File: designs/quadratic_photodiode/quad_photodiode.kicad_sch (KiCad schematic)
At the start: 56 parts, among them J1 Conn_Coaxial, J2 Conn_Coaxial, J3 Conn_Coaxial, J4 Conn_01x03_Female, U1 OPA356xxD, U2 OPA356xxD, U3 OPA356xxD, U4 OPA356xxD, U5 OPA356xxD, U6 OPA356xxD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

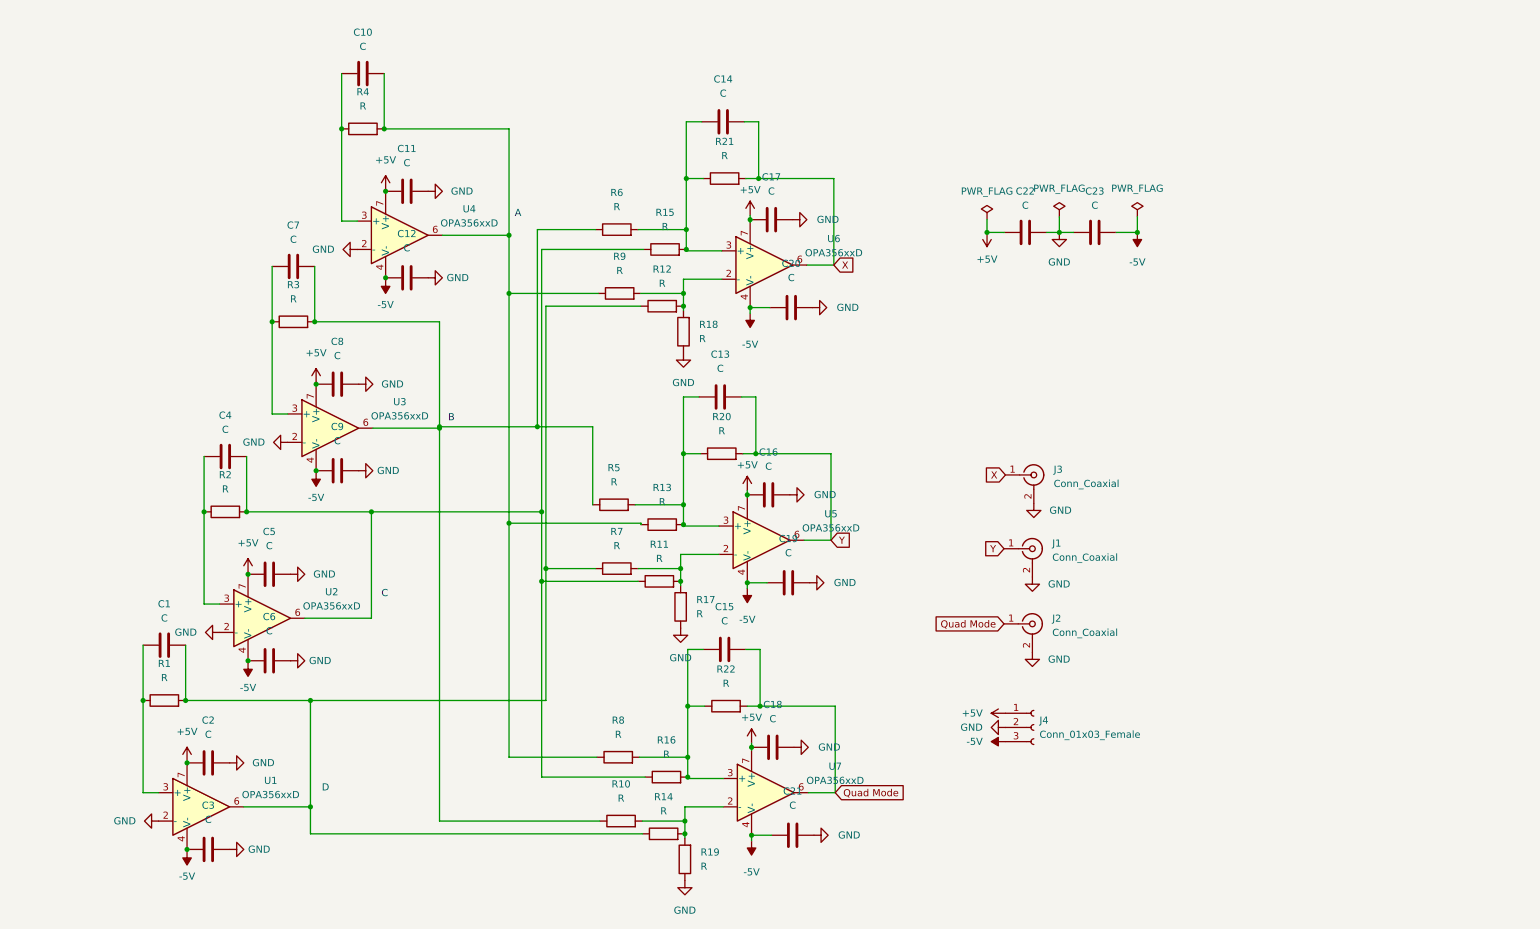
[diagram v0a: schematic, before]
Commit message: Updated schematic with better amplifier/pd
Used a circuit which stores four amplifiers and finally added the quadrant photodiode schematic.
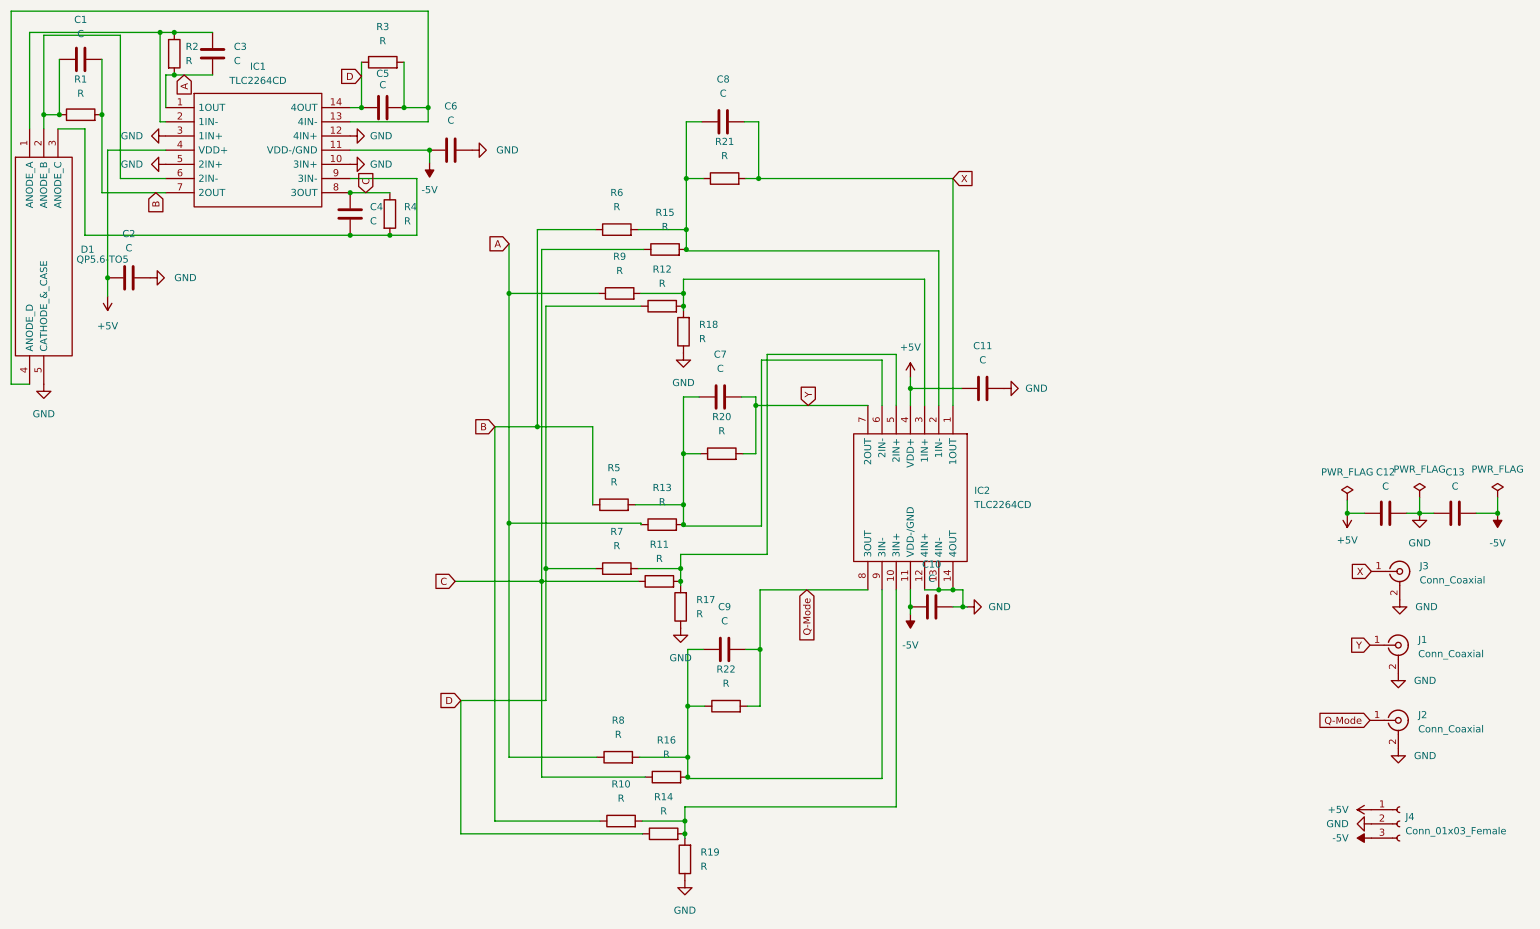
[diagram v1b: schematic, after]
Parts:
- removed C12, C16, C17, C18, C19, C20, C21, C7, C8, C9: C, symbol Device:C
- removed U1, U2, U3, U4, U5, U6, U7: OPA356xxD, Package_SO:SOIC-8_3.9x4.9mm_P1.27mm, symbol Amplifier_Operational:OPA356xxD
- added D1: QP5.6-TO5, quad_photodiode:QP586TO5, symbol QP5.6-TO5:QP5.6-TO5
- added IC1, IC2: TLC2264CD, quad_amplifier:SOIC127P600X175-14N, symbol TLC2264CD:TLC2264CD
- C1, C10, C11, C2, C3, C4, C5, C6: footprint (none) -> Capacitor_SMD:C_1206_3216Metric
- C12: renamed from C22; footprint (none) -> Capacitor_SMD:C_1206_3216Metric
- C13: renamed from C23; footprint (none) -> Capacitor_SMD:C_1206_3216Metric
- C7: renamed from C13; footprint (none) -> Capacitor_SMD:C_1206_3216Metric
- C8: renamed from C14; footprint (none) -> Capacitor_SMD:C_1206_3216Metric
- C9: renamed from C15; footprint (none) -> Capacitor_SMD:C_1206_3216Metric
- J1, J2, J3: footprint (none) -> Connector_Coaxial:SMA_Amphenol_901-144_Vertical
- J4: footprint (none) -> Connector_Molex:Molex_KK-254_AE-6410-03A_1x03_P2.54mm_Vertical
- R1, R10, R11, R12, R13, R14, R15, R16, R17, R18, R19, R2, R20, R21, R22, R3, R4, R5, R6, R7, R8, R9: footprint (none) -> Resistor_SMD:R_1206_3216Metric
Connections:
- net +5V: now also C2.2, IC1.4 (VDD+), IC2.4 (VDD+); no longer C2.1, C5.1
- net -5V: now also C10.1, C6.2, IC1.11 (VDD-/GND), IC2.11 (VDD-/GND); no longer C3.1, C6.1
- net GND: now also C10.2, C2.1, C6.1, D1.5 (CATHODE_&_CASE), IC1.10 (3IN+), IC1.12 (4IN+), IC1.3 (1IN+), IC1.5 (2IN+), IC2.12 (4IN+), IC2.13 (4IN-), IC2.14 (4OUT); no longer C2.2, C3.2, C5.2, C6.2
- net X: now also IC2.1 (1OUT)
- net Y: now also IC2.7 (2OUT)
- net A: now reaches R13.1, R8.1, R9.1
- net A: now also C3.2, R2.2, IC1.1 (1OUT); no longer C10.2, R4.2
- net at C7.1, R13.2, R20.1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: now also IC2.6 (2IN-)
- net C: now reaches R4.1
- net C: now also C4.2, R11.1, R15.1, R16.1, IC1.8 (3OUT); no longer C10.1
- net at R10.2, R14.2, R19.2: now also IC2.10 (3IN+)
- net at C9.1, R16.2, R22.1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: now also IC2.9 (3IN-)
- net D: now reaches R12.1, R14.1, R7.1
- net D: now also C5.2, R3.1, IC1.14 (4OUT); no longer C1.2, R1.2
- net B: now reaches R10.1, R5.1, R6.1
- net B: now also C1.2, R1.2, IC1.7 (2OUT); no longer R3.2
- net at R11.2, R17.2, R7.2: now also IC2.5 (2IN+)
- net at R12.2, R18.2, R9.2: now also IC2.3 (1IN+)
- net at C8.1, R15.2, R21.1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: now also IC2.2 (1IN-)
- net at C1.1, R1.1: now also D1.2 (ANODE_B), IC1.6 (2IN-)
- net at C4.1: now also R4.2, D1.3 (ANODE_C), IC1.9 (3IN-); no longer R2.1
- net Quad Mode renamed Q-Mode
- net Q-Mode: now also IC2.8 (3OUT)
- new net: C5.1, D1.4 (ANODE_D), IC1.13 (4IN-), R3.2
- new net: C3.1, D1.1 (ANODE_A), IC1.2 (1IN-), R2.1
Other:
- note removed: "A"
- note removed: "B"
- note removed: "C"
- note removed: "D"
- moved on the sheet: C12, C13, J1, J2, J3, J4
